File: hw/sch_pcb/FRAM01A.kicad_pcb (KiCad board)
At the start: 2 copper layers, 30 x 30 mm, 8 parts, among them IC1 CY15B108QN-40SXI, J1 HEADER_2x03_PARALLEL, J2 HEADER_2x04

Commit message: pcb layout update, ready for check
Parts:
- removed H1, H2, H3, H4: MountingHole_Pad, Mlab_Mechanical:MountingHole_3mm
- added C2: 100nF, Capacitor_SMD:C_0805_2012Metric, B.Cu at (139.8, 90.7)
- added D1: BZV55C-5,6V, Diode_SMD:D_SMA, B.Cu at (137.2, 78.0)
- added M1: HOLE M3, Mlab_Mechanical:MountingHole_3mm, F.Cu at (127.0, 76.2)
- added M2: HOLE M3, Mlab_Mechanical:MountingHole_3mm, F.Cu at (127.0, 96.5)
- added M3: HOLE, Mlab_Mechanical:MountingHole_3mm, F.Cu at (147.3, 76.2)
- added M4: HOLE, Mlab_Mechanical:MountingHole_3mm, F.Cu at (147.3, 96.5)
- C1: value 100nF -> 10uF; footprint Mlab_R:SMD-0805 -> Capacitor_SMD:C_0805_2012Metric
- J1: value HEADER_2x03_PARALLEL -> Umin ... Umax
- moved C1 2.81 mm to (139.7, 93.0)
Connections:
- net VDD renamed +3.3V
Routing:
- net +3.3V: track 44.9 -> 55.8 mm, vias 1 -> 0
- net ~{CS}: track 18.2 -> 17.4 mm, vias 0 -> 2
- net GND: vias 9 -> 12

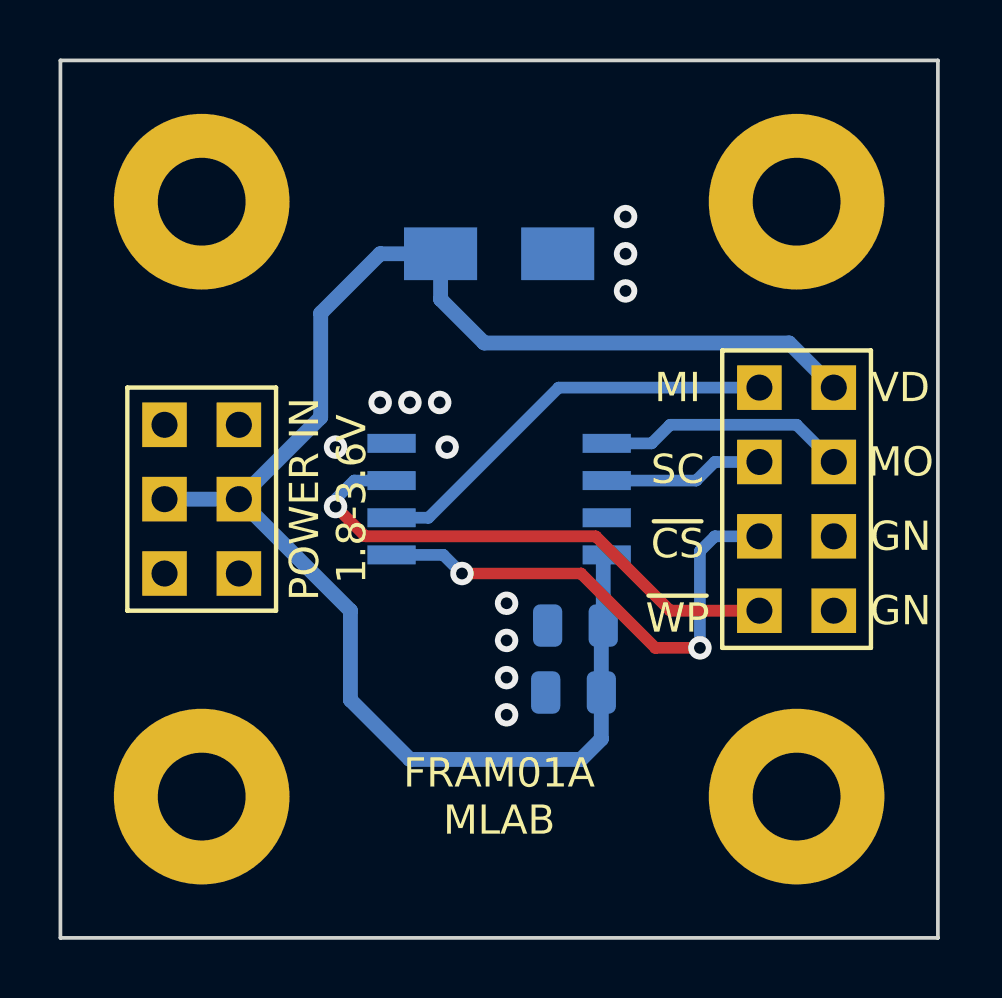
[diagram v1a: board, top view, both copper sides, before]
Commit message: smaller pcb layout 1x2
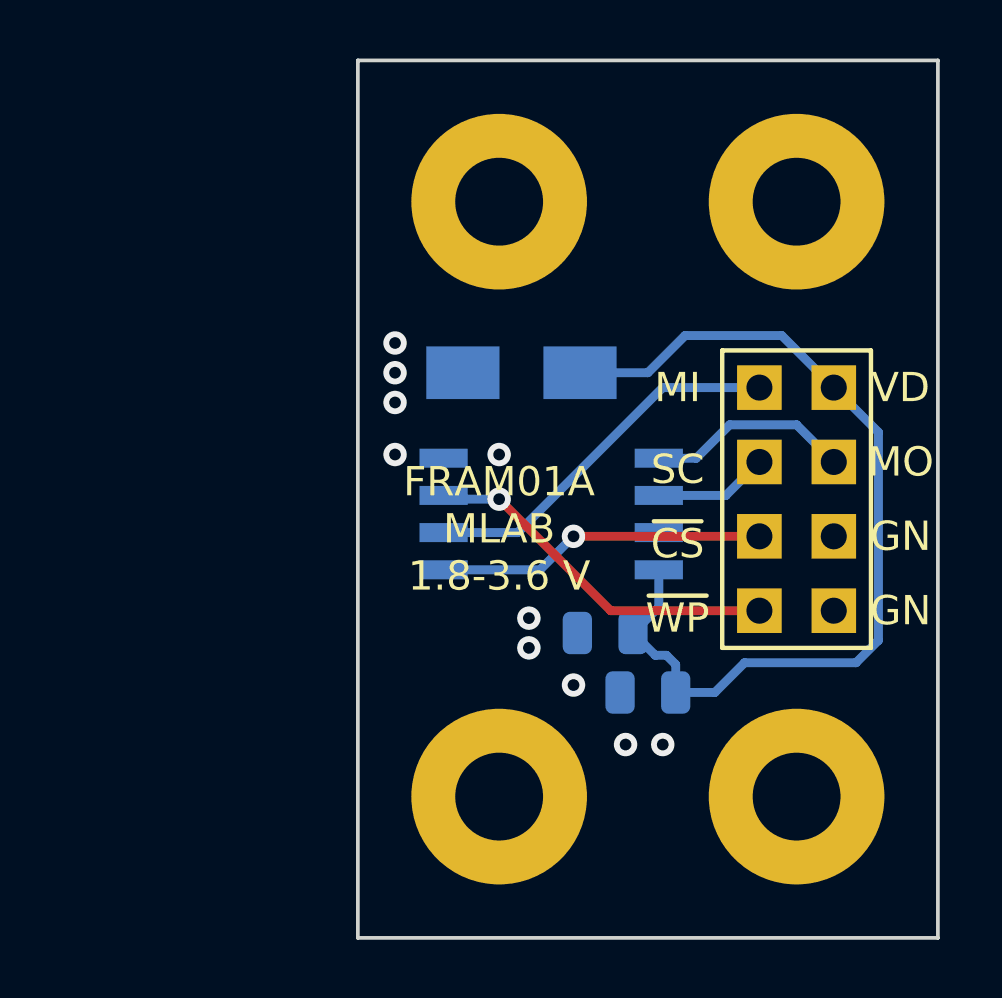
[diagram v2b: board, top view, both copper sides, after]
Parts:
- removed J1: Umin ... Umax, Mlab_Pin_Headers:Straight_2x03
- moved M1 10.2 mm to (137.2, 76.2)
- moved M2 10.2 mm to (137.2, 96.5)
- moved D1 4.13 mm to (137.9, 82.0), turned to 180 degrees
- moved C1 2.54 mm to (142.2, 93.0)
- moved IC1 1.85 mm to (138.9, 86.9)
- moved C2 1.05 mm to (140.8, 90.9)
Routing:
- net +3.3V: track 55.8 -> 32.3 mm
- net ~{CS}: track 17.4 -> 11.3 mm, vias 2 -> 1
- net ~{WP}: track 18.4 -> 12.4 mm
- net MISO: track 14.4 -> 12.8 mm
- net MOSI: track 8.54 -> 6.98 mm
- net SCK: track 5.48 -> 3.91 mm
- net GND: vias 12 -> 10
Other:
- board size 30 x 30 mm -> 19.8 x 30 mm
- board text added: "FRAM01A MLAB 1.8-3.6 V"
- board text removed: "FRAM01A MLAB"
- board text removed: "POWER IN 1.8-3.6V"

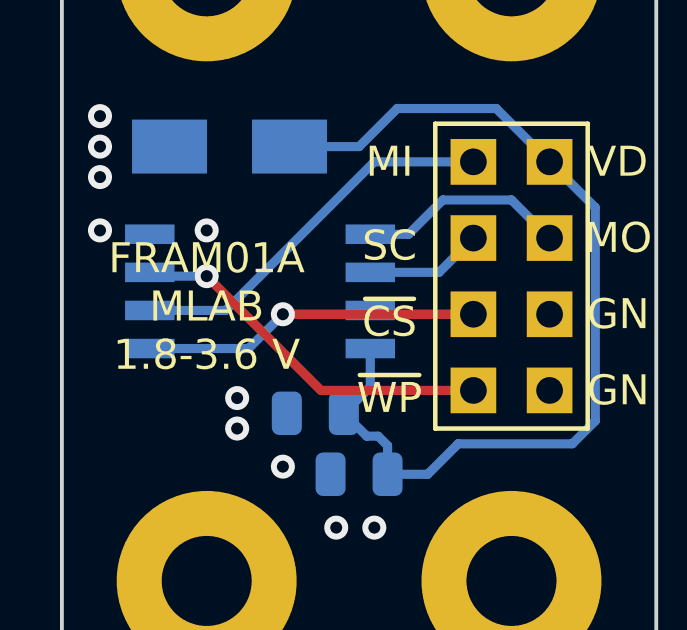
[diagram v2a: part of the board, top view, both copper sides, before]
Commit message: Fix DRC and ERC errors. Update title block.
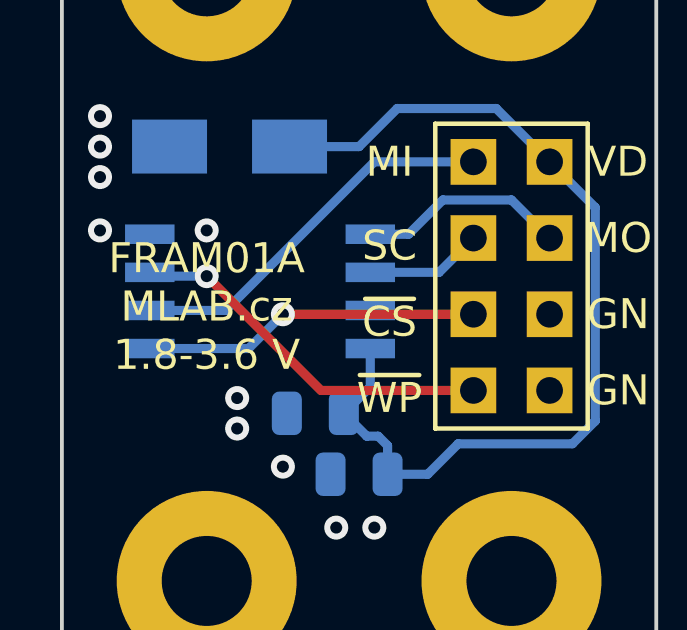
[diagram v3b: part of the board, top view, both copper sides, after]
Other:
- board text added: "FRAM01A MLAB.cz 1.8-3.6 V"
- board text removed: "FRAM01A MLAB 1.8-3.6 V"
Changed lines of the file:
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@@
     (effects (font (size 1 1) (thickness 0.15)))
   )
-  (gr_text "FRAM01A\nMLAB\n1.8-3.6 V" (at 137.16 87.376) (layer "F.SilkS")
+  (gr_text "FRAM01A\nMLAB.cz\n1.8-3.6 V" (at 137.16 87.376) (layer "F.SilkS")
     (effects (font (size 1 1) (thickness 0.15)))
   )
@@
     (pts (xy 152.146 101.346) (xy 152.146 71.374))
     (height 2.794)
-    (gr_text "1180.0000 mils" (at 153.79 86.36 90) (layer "Dwgs.User")
+    (gr_text "1180,0000 mils" (at 153.79 86.36 90) (layer "Dwgs.User")
       (effects (font (size 1 1) (thickness 0.15)))
     )
@@
     (pts (xy 137.16 96.52) (xy 147.32 96.52))
     (height 7.62)
-    (gr_text "400.0000 mils" (at 142.24 102.99) (layer "Dwgs.User")
+    (gr_text "400,0000 mils" (at 142.24 102.99) (layer "Dwgs.User")
       (effects (font (size 1 1) (thickness 0.15)))
     )
@@
     (pts (xy 137.16 76.2) (xy 137.16 96.52))
     (height 7.62)
-    (gr_text "800.0000 mils" (at 128.39 86.36 90) (layer "Dwgs.User")
+    (gr_text "800,0000 mils" (at 128.39 86.36 90) (layer "Dwgs.User")
       (effects (font (size 1 1) (thickness 0.15)))
     )
@@
     (pts (xy 132.334 71.374) (xy 152.146 71.374))
     (height -2.794)
-    (gr_text "780.0000 mils" (at 142.24 67.43) (layer "Dwgs.User")
+    (gr_text "780,0000 mils" (at 142.24 67.43) (layer "Dwgs.User")
       (effects (font (size 1 1) (thickness 0.15)))
     )
@@
   (segment (start 143.19 92.009) (end 143.19 92.964) (width 0.3048) (layer "B.Cu") (net 8))
   (segment (start 141.732 90.932) (end 142.613 90.051) (width 0.3048) (layer "B.Cu") (net 8))
-  (segment (start 142.6845 88.8445) (end 142.613 88.773) (width 0.25) (layer "B.Cu") (net 8))
   (segment (start 143.51 80.772) (end 142.24 82.042) (width 0.3048) (layer "B.Cu") (net 8))
   (segment (start 150.114 91.186) (end 149.352 91.948) (width 0.3048) (layer "B.Cu") (net 8))
